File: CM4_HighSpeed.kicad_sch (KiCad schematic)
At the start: 14 parts, among them J12 THD-02-R, J13 1-2199119-5, J14 USB_A, J15 USB_OTG, J16 Conn_01x02, J2 SS-52400-004, J5 690-019-298-412, U11 TPD4EUSB30, U13 RT9742SNGV

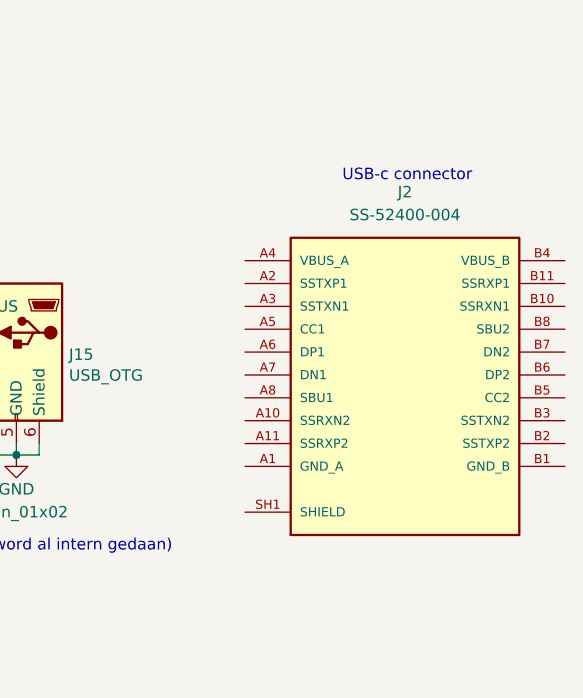
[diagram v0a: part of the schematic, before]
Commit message: USB-c toegeveogd moet alleen nog omvormen
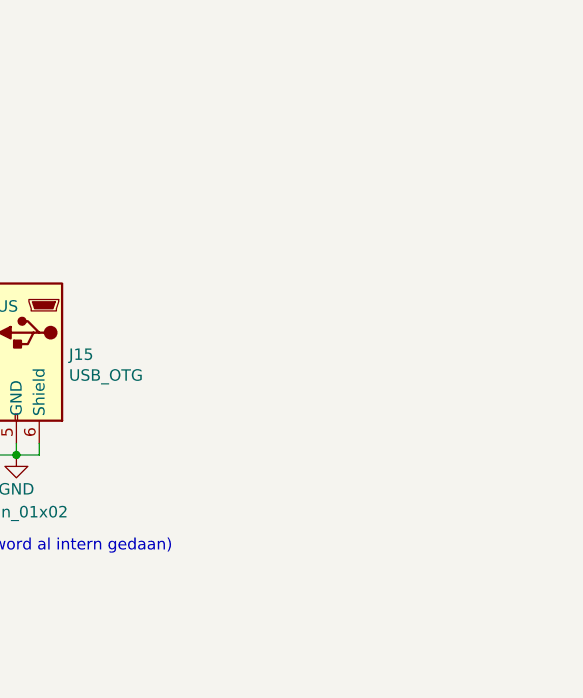
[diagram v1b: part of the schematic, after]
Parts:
- removed J2: SS-52400-004, SS-52400-004:STEWART_SS-52400-004 (USB-C), symbol SS-52400-004:SS-52400-004
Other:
- note removed: "USB-c connector"

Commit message: Heb mijn documentatie geleverd voor de USB-c en heb een BOM toegevoegd
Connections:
- net +5v renamed +5V DC
- net P7 renamed +3,3V DC
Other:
- moved on the sheet: C56, C57, U13
